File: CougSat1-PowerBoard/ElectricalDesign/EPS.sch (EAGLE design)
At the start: 217 parts, among them J1 PV0, J2 PV1, J3 PV2, J4 PV3, J5 Umbilical, J6 SWD, J7 CougSat Card, J8 Deployables, Q1 NTLUD3A50PZ, Q10 DMN2008LFU, Q11 DMN2008LFU, Q12 CSD25402Q3A, Q13 CSD25402Q3A, Q14 NTLUD3A50PZ, Q15 NTLUD3A50PZ, Q16 NTLUD3A50PZ, Q17 NTLUD3A50PZ, Q18 NTLUD3A50PZ, Q19 NTLUD3A50PZ, Q2 NTLUD3A50PZ, Q20 NTLUD3A50PZ, Q21 NTLUD3A50PZ, Q22 NTLUD3A50PZ, Q23 CSD25402Q3A, Q24 CSD25402Q3A, Q25 DMN53D0L, Q26 NTLUD3A50PZ, Q27 NTLUD3A50PZ, Q28 NTLUD3A50PZ, Q29 NTLUD3A50PZ, Q3 NTLUD3A50PZ, Q30 NTLUD3A50PZ, Q31 NTLUD3A50PZ, Q32 NTLUD3A50PZ, Q33 NTLUD3A50PZ, Q34 NTLUD3A50PZ, Q35 NTLUD3A50PZ, Q36 NTLUD3A50PZ, Q37 NTLUD3A50PZ, Q38 NTLUD3A50PZ, Q39 NTLUD3A50PZ, Q4 NTLUD3A50PZ, Q40 NTLUD3A50PZ, Q41 NTLUD3A50PZ, Q42 NTLUD3A50PZ, Q43 NTLUD3A50PZ, Q5 NTLUD3A50PZ, Q6 NTLUD3A50PZ, Q7 NTLUD3A50PZ, Q8 NTLUD3A50PZ, Q9 NTLUD3A50PZ, SW1 D2MQ-1-TL, U1 BQ29700, U10 LTC2499, U11 LTC2499, U12 LTC2499, U13 LTC2499, U14 MCP1501-18, U15 LTC2499, U2 BQ29700, U3 TPS64200, U4 TPS64200, U5 STM32L476RGT, U6 TCA9535R, U7 SN74LVC244AR, U8 TCA9535R, U9 LTC2499

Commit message: Added JTAG Disconnector and LEDs
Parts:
- added C41: 100nF 10%, CougsInSpace-Capacitors:CAP-V-100NF-1608
- added D7, D8: LTC4411, CougsInSpace-DiscreteSemi:LTC4411
- added DS1, DS2: Green, CougsInSpace-LEDs:LED-H-GRN-1608
- added DS3, DS4, DS5: Green, CougsInSpace-LEDs:LED-V-GRN-1608
- added R69: 10kΩ 0.1%, CougsInSpace-Resistors:RES-V-10K-1608
- added R70: 50mΩ 1%, CougsInSpace-Resistors:RES-V-0.05R-1608
- added R73, R74: 1kΩ 0.1%, CougsInSpace-Resistors:RES-H-1K-1608
- added R75, R76, R77: 1kΩ 0.1%, CougsInSpace-Resistors:RES-V-1K-1608
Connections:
- net BATT_PROTECT_VSS-A renamed BP_VSS-A
- new net 3.3V_LED-A: DS4.C, R76.2
- new net 3.3V_LED-B: DS3.C, R75.2
- new net PMIC_LED-A: DS5.A, U5BASE.EXTRA_PIN
- new net PMIC_LED-C: DS5.C, R77.2
- new net VBATT: D7.OUT, D8.OUT, U5BASE.VBAT
- new net VBATT_LED-A: DS1.C, R73.1
- new net VBATT_LED-B: DS2.C, R74.1
- net 3.3V: now also C41.1, R69.2, U7E1.VCC
- net 3.3V-A: now also DS4.A
- net 3.3V-B: now also DS3.A
- net AGND: no longer R61.1
- net BUS_JTAG_TCK: now also U7E1.A1
- net BUS_JTAG_TDI: now also U7E1.A2
- net BUS_JTAG_TDO: now also U7E2.Y3
- net BUS_JTAG_TMS: now also U7E1.A3
- net CHASSIS: now also R61.1
- net DGND: now also C41.2, R77.1, U7E1.A4, U7E1.GND, U7E1.Y4, U7E2.A1, U7E2.A2, U7E2.A4, U7E2.Y1, U7E2.Y2, U7E2.Y4
- net I_DEPLOY: now also R70.2
- net JTAG_EN_PMIC: now also R69.1, U7E1.!EN, U7E2.!EN
- net JTAG_TCK: now also U7E1.Y1
- net JTAG_TDI: now also U7E1.Y2
- net JTAG_TDO: now also U7E2.A3
- net JTAG_TMS: now also U7E1.Y3
- net PGND: now also D7.CTL, D7.GND, D8.CTL, D8.GND, R73.2, R74.2, R75.1, R76.1
- net PR_DEPLOY: now also R70.1
- net VBATT-A: now also D7.IN, DS1.A
- net VBATT-B: now also D8.IN, DS2.A
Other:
- note added: "4A3>"
- note added: "4A5>"
- note added: "8A3>"
- note added: "8B1> 8B5>"
- note added: "8B6>"
- note added: "9B5>"
- note added: "9xx> 10xx> 4C5> 5A1> 7B1> 7C1> 7D1>"
- note added: "9xx> 10xx> 4C5> 5C1> 7B1> 7C1> 7D1>"
- note added: "<8A1"
- note added: "<8B1 <8C5"
- note added: "<8B1> <8C5"
- note added: "<8B5 <8C6"
- note added: "<8C5"
- note added: "<8C6"
- note added: "Note: 1/3.3 Voltage divider allows inputs up to ±5.4V"
- note added: "Note: Each power rail channel (PR_) is rated for 1A PR_DEPLOY is rated for 2A Currents shown are the expected consumption"
- note added: "Note: Fix all off sheet designators linked to this sheet Note: All signals above are GPIO, connect to any GPIO bank, whichever is best for routing"
- note added: "Note: PR_DEPLOY is rated for 2A"
- note removed: "8B5> 8xx>"
- note removed: "9xx> 10xx> 5A1> 7B1> 7C1> 7D1>"
- note removed: "9xx> 10xx> 5C1> 7B1> 7C1> 7D1>"
- note removed: "<4B3"
- note removed: "<8B5 <8xx"
- note removed: "<8B5> <8xx"
- note removed: "Note: Each power rail channel (PR_) is rated for 1A. Currents shown are the expected consumption"
- note removed: "Note: Fix all off sheet designators linked to this sheet Note: All signals above are GPIO, connect to any GPIO bank, whichever is best for routing, don't use PD2"
- moved on the sheet: C18, C19, C20, C21, C22, C23, C24, C31, C36, C37, C38, FB1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

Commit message: Added Switching Defaults
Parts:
- added RN1, RN10, RN11, RN12, RN13, RN14, RN15, RN16, RN17, RN18, RN2, RN3, RN4, RN5, RN6, RN7, RN8, RN9: 10kΩ 1%, CougsInSpace-Resistors:RES-4-V-10K-1632
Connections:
- net 3.3V: now also RN10A.2, RN10B.2, RN10C.2, RN10D.2, RN11A.2, RN11B.2, RN11C.2, RN11D.2, RN12A.2, RN12B.2, RN17C.2, RN17D.2, RN18C.2, RN18D.2, RN8C.2, RN8D.2, RN9A.2, RN9B.2, RN9C.2, RN9D.2
- net PC_3.3V-0A: now also RN5A.2
- net PC_3.3V-0B: now also RN5B.2
- net PC_3.3V-10A: now also RN8C.1
- net PC_3.3V-10B: now also RN8D.1
- net PC_3.3V-11A: now also RN17C.1
- net PC_3.3V-11B: now also RN17D.1
- net PC_3.3V-12A: now also RN18C.1
- net PC_3.3V-12B: now also RN18D.1
- net PC_3.3V-1A: now also RN5C.2
- net PC_3.3V-1B: now also RN5D.2
- net PC_3.3V-2A: now also RN6A.2
- net PC_3.3V-2B: now also RN6B.2
- net PC_3.3V-3A: now also RN6C.2
- net PC_3.3V-3B: now also RN6D.2
- net PC_3.3V-4A: now also RN7A.2
- net PC_3.3V-4B: now also RN7B.2
- net PC_3.3V-5A: now also RN7C.2
- net PC_3.3V-5B: now also RN7D.2
- net PC_3.3V-6A: now also RN8A.2
- net PC_3.3V-6B: now also RN8B.2
- net PC_3.3V-7A: now also RN11A.1
- net PC_3.3V-7B: now also RN11B.1
- net PC_3.3V-8A: now also RN11C.1
- net PC_3.3V-8B: now also RN11D.1
- net PC_3.3V-9A: now also RN12A.1
- net PC_3.3V-9B: now also RN12B.1
- net PC_BATT-0A: now also RN16C.2
- net PC_BATT-0B: now also RN16D.2
- net PC_BATT-1A: now also RN17A.2
- net PC_BATT-1B: now also RN17B.2
- net PC_BATT-2A: now also RN12C.1
- net PC_BATT-2B: now also RN12D.1
- net PC_BATT-3A: now also RN16A.1
- net PC_BATT-3B: now also RN16B.1
- net PC_BATT-4A: now also RN13A.1
- net PC_BATT-4B: now also RN13B.1
- net PC_BATT-5A: now also RN13C.1
- net PC_BATT-5B: now also RN13D.1
- net PC_BATT-6A: now also RN14A.1
- net PC_BATT-6B: now also RN14B.1
- net PC_BH-0A: now also RN14C.1
- net PC_BH-0B: now also RN14D.1
- net PC_BH-1A: now also RN15A.1
- net PC_BH-1B: now also RN15B.1
- net PC_DEPLOY-A: now also RN15C.1
- net PC_DEPLOY-B: now also RN15D.1
- net PGND: now also RN16C.1, RN16D.1, RN17A.1, RN17B.1, RN1A.1, RN1B.1, RN1C.1, RN1D.1, RN2A.1, RN2B.1, RN2C.1, RN2D.1, RN3A.1, RN3B.1, RN3C.1, RN3D.1, RN4A.1, RN4B.1, RN4C.1, RN4D.1, RN5A.1, RN5B.1, RN5C.1, RN5D.1, RN6A.1, RN6B.1, RN6C.1, RN6D.1, RN7A.1, RN7B.1, RN7C.1, RN7D.1, RN8A.1, RN8B.1
- net PVC_3.3V-0A: now also RN9A.1
- net PVC_3.3V-0B: now also RN9B.1
- net PVC_3.3V-1A: now also RN9C.1
- net PVC_3.3V-1B: now also RN9D.1
- net PVC_3.3V-2A: now also RN10A.1
- net PVC_3.3V-2B: now also RN10B.1
- net PVC_3.3V-3A: now also RN10C.1
- net PVC_3.3V-3B: now also RN10D.1
- net PV_SW-0A: now also RN1A.2
- net PV_SW-0B: now also RN1B.2
- net PV_SW-1A: now also RN1C.2
- net PV_SW-1B: now also RN1D.2
- net PV_SW-2A: now also RN2A.2
- net PV_SW-2B: now also RN2B.2
- net PV_SW-3A: now also RN2C.2
- net PV_SW-3B: now also RN2D.2
- net PV_SW-4A: now also RN3A.2
- net PV_SW-4B: now also RN3B.2
- net PV_SW-5A: now also RN3C.2
- net PV_SW-5B: now also RN3D.2
- net PV_SW-6A: now also RN4A.2
- net PV_SW-6B: now also RN4B.2
- net PV_SW-7A: now also RN4C.2
- net PV_SW-7B: now also RN4D.2
- net UMB_SW-A: now also RN18A.1
- net UMB_SW-B: now also RN18B.1
- net VBATT: now also RN12C.2, RN12D.2, RN13A.2, RN13B.2, RN13C.2, RN13D.2, RN14A.2, RN14B.2, RN14C.2, RN14D.2, RN15A.2, RN15B.2, RN15C.2, RN15D.2, RN16A.2, RN16B.2, RN18A.2, RN18B.2
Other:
- note added: "10B5>"
- note added: "3A2> 3B2> 3C2> 9C1> 9C3> 10A3> 10A5> 10C3> 10C5> 11A3> 11C3>"
- note added: "9A1>"
- note added: "9A3>"
- note added: "9B1> 9B5>"
- note added: "9B4>"
- note added: "9B6>"
- note added: "<10B5"
- note added: "<10B5>"
- note added: "<3A2> <3B2> <3C2> <9C1> <9C3> <10A3> <10A5> <10C3> <10C5> <11A3> <11C3>"
- note added: "<9A1"
- note added: "<9A1>"
- note added: "<9A3"
- note added: "<9A5"
- note added: "<9A5 <9xx>"
- note added: "<9A5>"
- note added: "<9B1 <9C5"
- note added: "<9B1> <9C5"
- note added: "<9B4"
- note added: "<9B4>"
- note added: "<9B5 <9C6"
- note added: "<9C5"
- note added: "<9C6"
- note added: "Note: Bus outputs ON from both batteries or regulators"
- note added: "Note: Fix all off sheet designators linked to this sheet Note: Resistors can be rearranged or replaced with single resistors, whichever is best for routing"
- note added: "Note: PV input ON to both batteries"
- note added: "Note: PV monitoring, & payload 3.3V OFF"
- note added: "Note: Payload Vbatt, battery heaters, deployables, & umbilical input OFF"
- note added: "Note: These are the default states of the power rails When the PMIC does not drive the switches, these rails are on/off This occurs when the PMIC is reset or being programmed"
- note added: "Page 10, 11"
- note added: "Page 10: Backplane Digital & ADCs Page 11: ADCs Page 12: Mechanical Layout"
- note added: "Page 1: Block Diagram Page 2: Power Rails Page 3: Input Switching Matrix Page 4: Batteries Page 5: 3.3V Regulation Page 6: Output Switching Matrix Page 7: Output Switching Matrix Page 8: Switching Default States Page 9: PMIC"
- note added: "Page 3, 8"
- note added: "Page 6, 10"
- note added: "Page 9"
- note added: "Pages 6, 7, 8"
- note removed: "3A2> 3B2> 3C2> 8C1> 8C3> 9A3> 9A5> 9C3> 9C5> 10A3> 10C3>"
- note removed: "8A1>"
- note removed: "8A3>"
- note removed: "8B1> 8B5>"
- note removed: "8B4>"
- note removed: "8B6>"
- note removed: "9B5>"
- note removed: "<3A2> <3B2> <3C2> <8C1> <8C3> <9A3> <9A5> <9C3> <9C5> <10A3> <10C3>"
- note removed: "<8A1"
- note removed: "<8A1>"
- note removed: "<8A3"
- note removed: "<8A5"
- note removed: "<8A5 <9xx>"
- note removed: "<8A5>"
- note removed: "<8B1 <8C5"
- note removed: "<8B1> <8C5"
- note removed: "<8B4"
- note removed: "<8B4>"
- note removed: "<8B5 <8C6"
- note removed: "<8C5"
- note removed: "<8C6"
- note removed: "<8xx"
- note removed: "<9B5>"
- note removed: "Page 10: ADCs Page 11: Mechanical Layout"
- note removed: "Page 1: Block Diagram Page 2: Power Rails Page 3: Input Switching Matrix Page 4: Batteries Page 5: 3.3V Regulation Page 6: Output Switching Matrix Page 7: Output Switching Matrix Page 8: PMIC Page 9: Backplane Digital & ADCs"
- note removed: "Page 6, 9"
- note removed: "Page 8"
- note removed: "Page 9, 10"
- note removed: "Pages 6, 7"

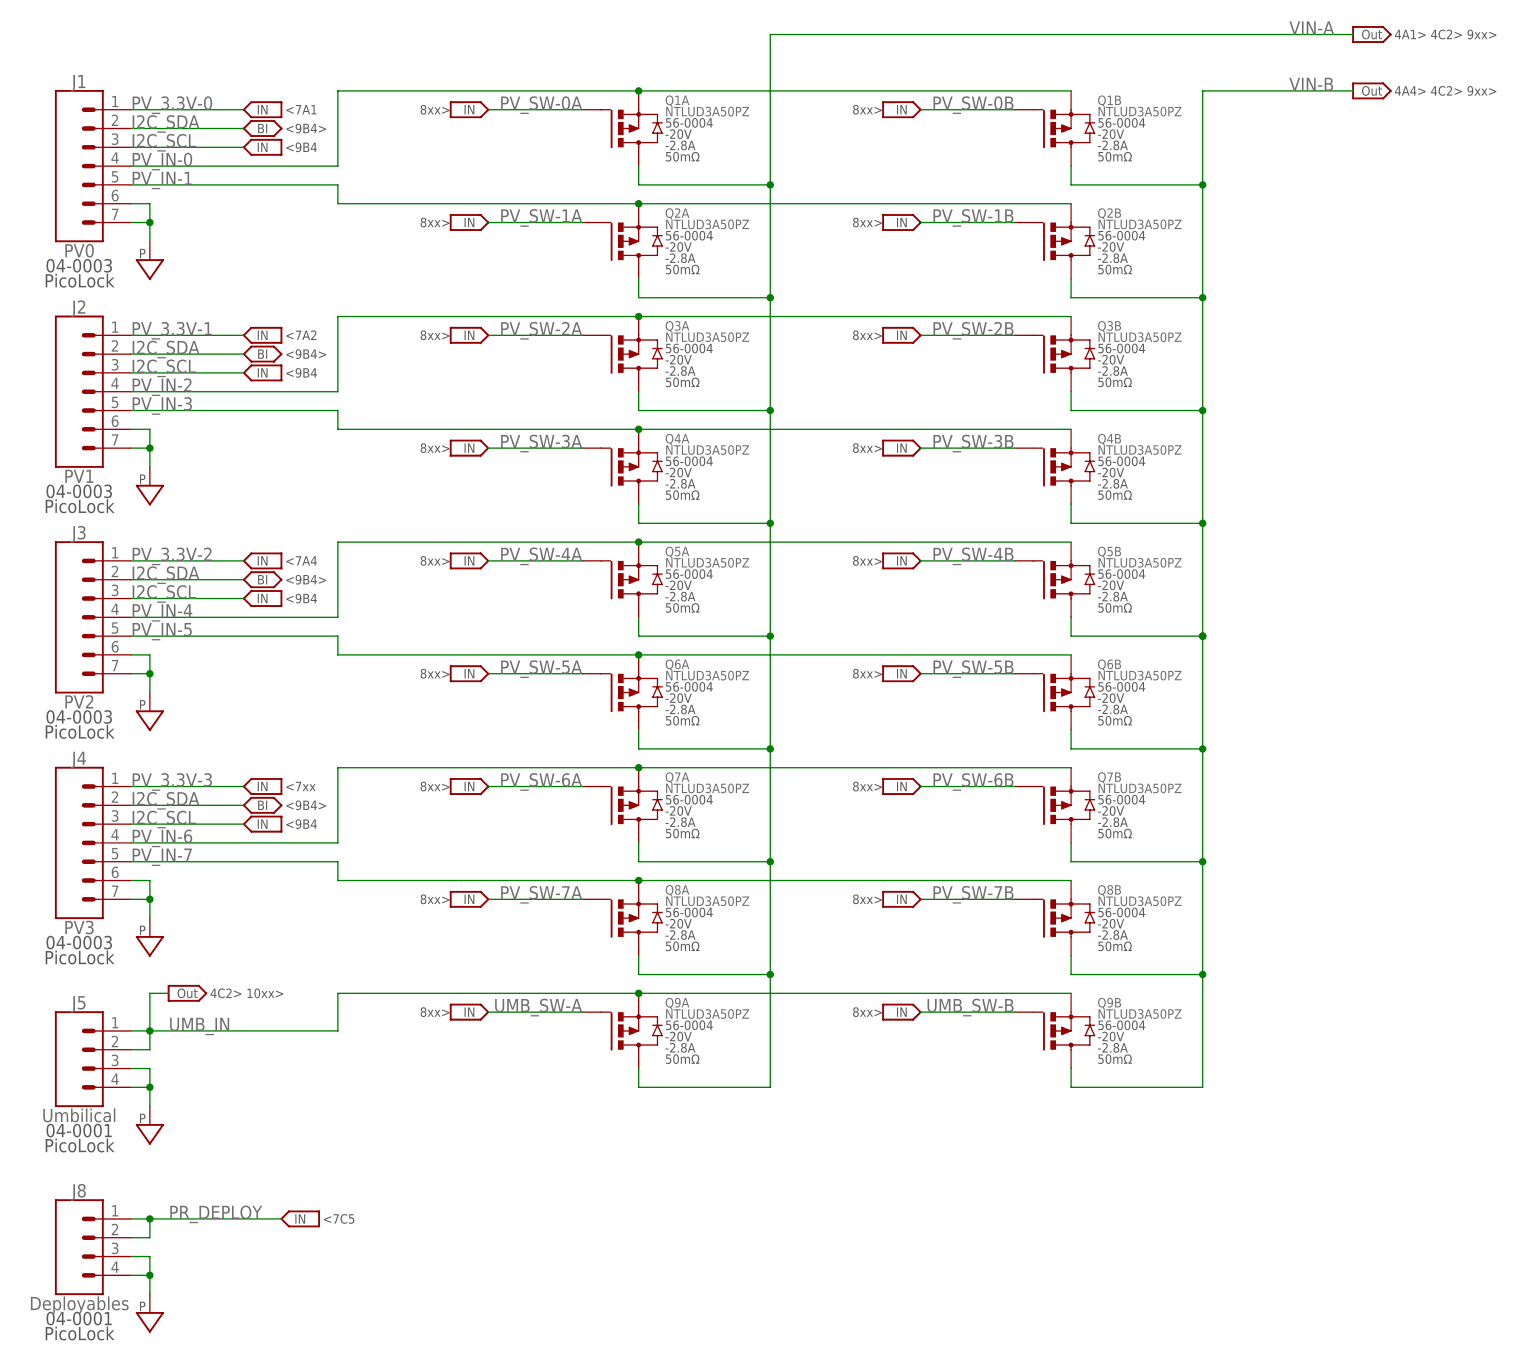
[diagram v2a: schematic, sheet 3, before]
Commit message: Wrote Schematic Documentation
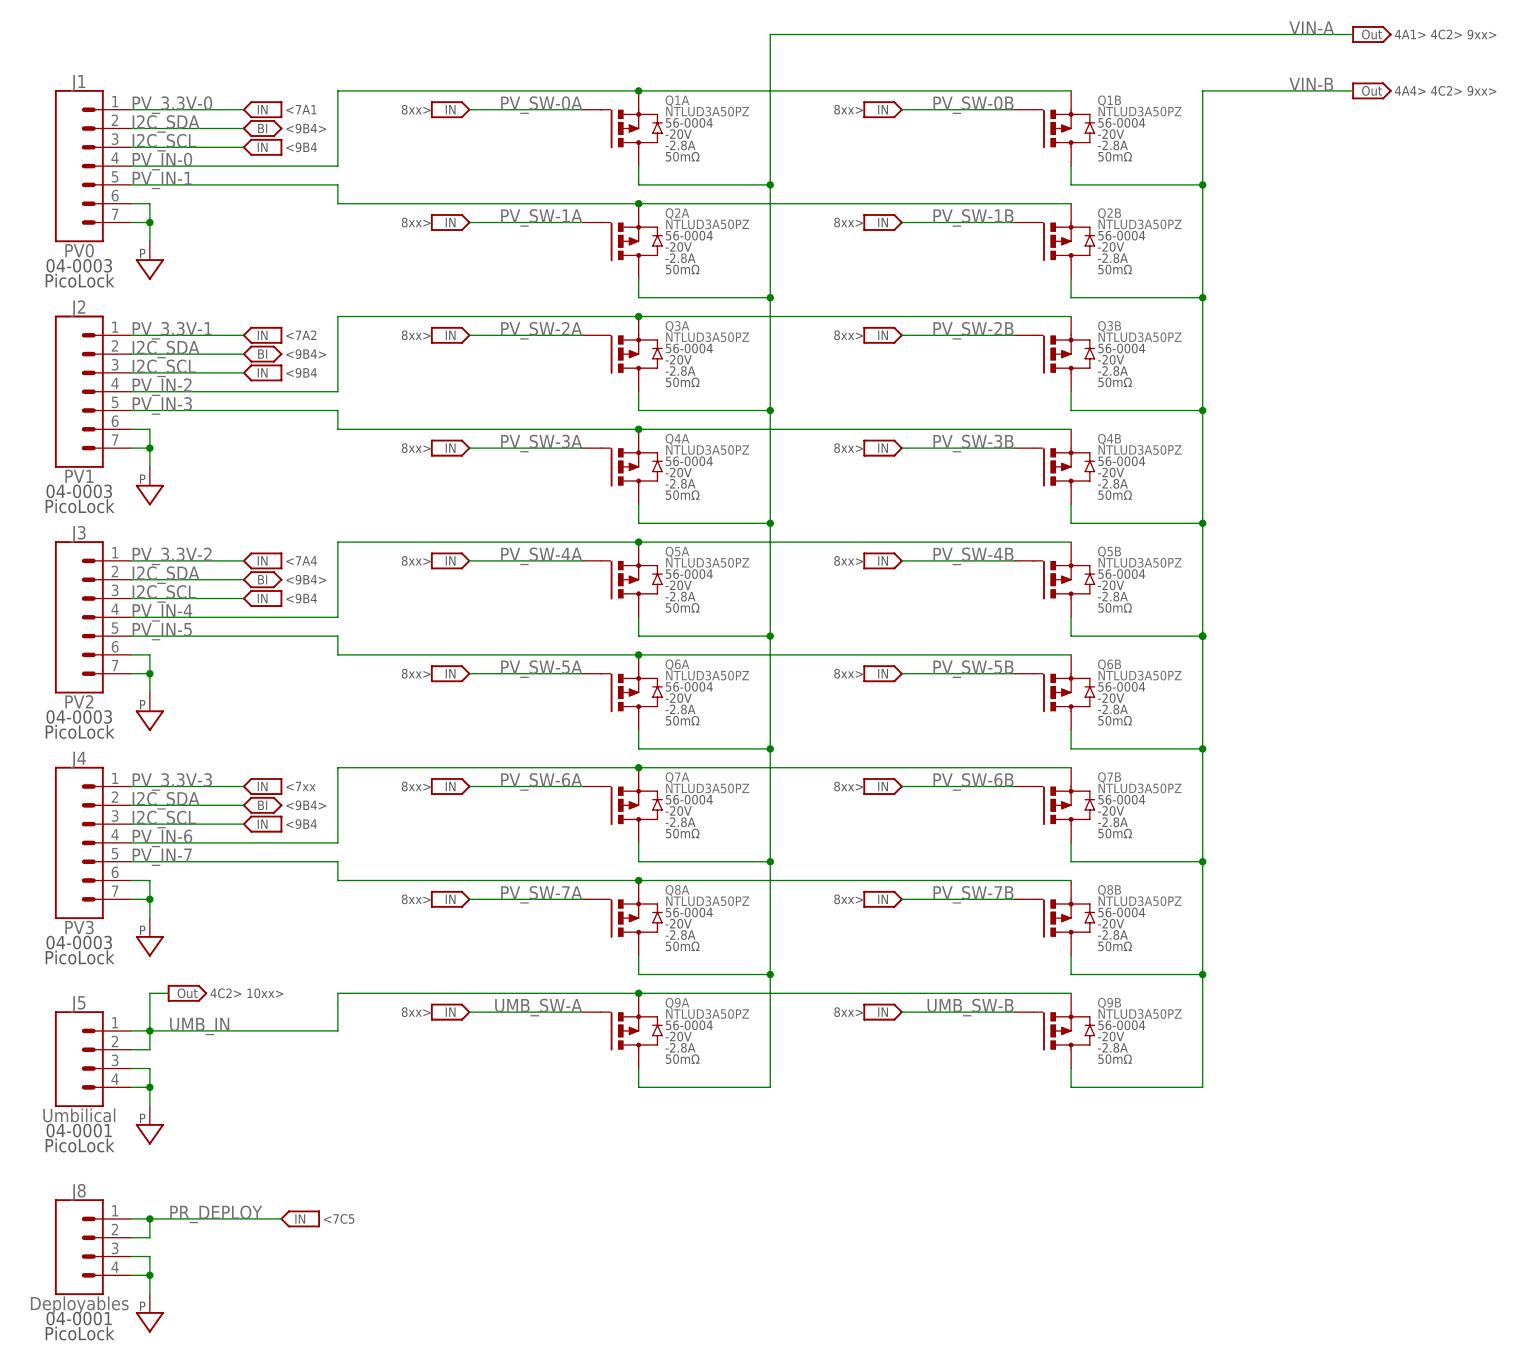
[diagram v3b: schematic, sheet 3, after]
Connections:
- net 3.3V: now also U11.CA0, U13.CA0
- net DGND: now also U11.CA1, U12.CA2, U13.CA2, U15.CA0; no longer U11.CA0, U13.CA0, U13.CA1
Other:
- note added: "Note: Addr = 0x2C | R/!W"
- note added: "Note: Addr = 0x72 | R/!W"
- note added: "Note: Addr = 0x74 | R/!W"
- note removed: "Note: Addr = 0x48 | R/!W"
- note removed: "Note: Addr = 0x6A | R/!W"
- note removed: "Note: Addr = 0x8A | R/!W"
